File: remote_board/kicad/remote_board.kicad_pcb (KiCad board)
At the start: 2 copper layers, 99 x 99 mm, 35 parts, among them U1 WeMos_D1_mini

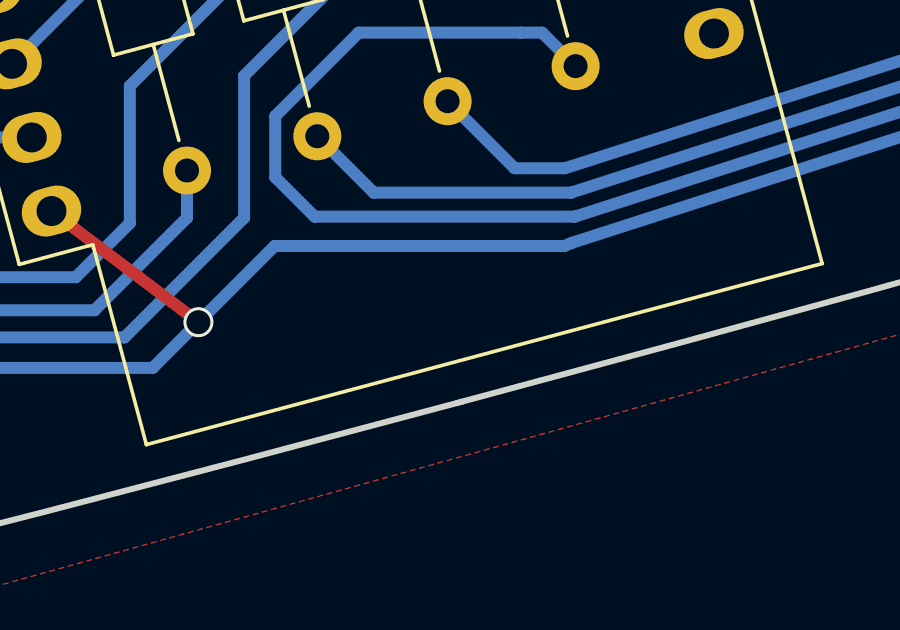
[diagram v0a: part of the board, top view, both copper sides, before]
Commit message: change in PCB design for fab needs
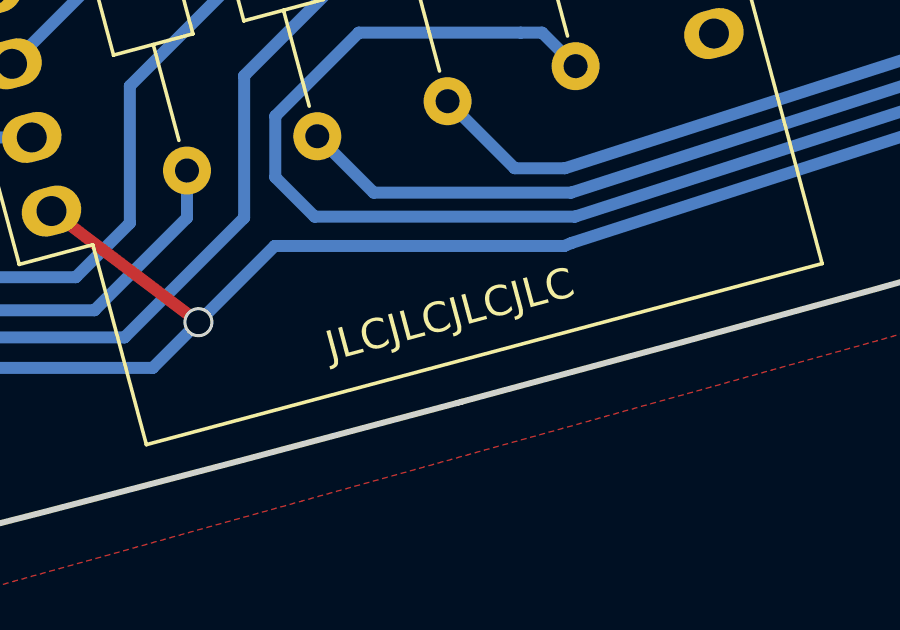
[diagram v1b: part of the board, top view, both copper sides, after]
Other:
- board text added: "JLCJLCJLCJLC"
